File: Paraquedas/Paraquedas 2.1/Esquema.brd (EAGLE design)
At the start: 67.5 x 58.3 mm, 20 parts, among them Q1 IRF540, Q2 IRF540, Q3 IRF540

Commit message: Message
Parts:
- removed LED3: 5mm, led:LED5MM
- removed R8: 220, rcl:0207/10
- added LED2: 5mm, led:LED5MM
- added R7: 1k, rcl:0207/10
- R1, R5: value 220 -> 1k
- moved R4 97.4 mm to (-14.0, 11.4)
- moved R2 96.9 mm to (-14.0, 1.27), flipped to the bottom, turned to 180 degrees
- moved R3 96.7 mm to (-14.0, 6.35)
- moved LED1 47.7 mm to (13.5, 33.9), turned to 0 degrees
- moved R5 47.2 mm to (5.08, 40.6), turned to 270 degrees
- moved Q2 46.4 mm to (55.9, 25.4), flipped to the top
- moved SKIB2 46.4 mm to (55.9, 49.5), flipped to the top
- moved U$2 42.0 mm to (53.3, 6.35)
- moved R6 39.1 mm to (12.7, 26.0)
- moved R1 38.3 mm to (13.6, 50.3)
- moved OK2 36.8 mm to (15.2, 17.8)
- moved OK1 36.7 mm to (15.2, 43.2)
- moved U$1 25.0 mm to (44.5, 6.35)
- moved Q1 21.2 mm to (43.2, 25.4), flipped to the top
- moved SKIB1 21.2 mm to (43.2, 49.5), flipped to the top
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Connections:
- removed net N$3 (its old number): LED3.A, R8.2
- new net N$1: LED2.A, R7.2
- net GND: now also LED2.K; no longer LED3.K
- net SINAL_SKIB1: no longer R5.1
- net SINAL_SKIB2: no longer R8.1
- net SKIB1: now also U$2.1; no longer U$2.2
- net SKIB1_CONECTOR: now also R5.1
- net SKIB2: now also U$2.2; no longer U$2.1
- net SKIB2_CONECTOR: now also R7.1
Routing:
- net GND: track 0.00 -> 22.9 mm, vias 0 -> 4
- net SKIB1_CONECTOR: track 68.0 -> 89.4 mm
- net SKIB2_CONECTOR: track 77.3 -> 98.1 mm
- net 3.3V: track 68.2 -> 88.0 mm
- net SINAL_SKIB2: track 13.6 -> 0.00 mm
- net SINAL_SKIB1: track 13.2 -> 0.00 mm
- net N$1: track 0.00 -> 9.23 mm
- net N$3 (its old number): track 6.07 -> 0.00 mm
- net VCC: track 80.5 -> 86.2 mm
- net N$4: track 13.9 -> 11.1 mm
- net N$3: track 5.99 -> 7.80 mm
- net SKIB2: track 11.8 -> 13.2 mm
- net BUZZER: track 24.7 -> 23.5 mm
- net N$5: track 12.9 -> 11.8 mm
- net SKIB1: track 19.0 -> 19.7 mm
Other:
- board size 67.5 x 58.3 mm -> 66 x 57.2 mm

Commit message: Update paraquedas
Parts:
- removed LED1, LED2: 5mm, led:LED5MM
- removed OK1: PC817, optocoupler:DIL04
- added GND: PC817, optocoupler:DIL04
- added LSKIB1, LSKIB2: 5mm, led:LED5MM
- moved BATERIA 22.9 mm to (54.9, 7.37)
- moved R7 14.0 mm to (19.2, 18.2)
- moved R5 12.7 mm to (17.8, 40.6)
- moved U$1 8.98 mm to (35.6, 7.62), turned to 180 degrees
- moved U$2 8.98 mm to (44.5, 7.62)
- moved OK2 4.02 mm to (11.4, 19.1), turned to 270 degrees
- moved R1 3.41 mm to (10.5, 48.8), turned to 0 degrees
- moved R6 1.27 mm to (14.0, 26.0), turned to 0 degrees
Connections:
- net 3.3V: now also GND.4; no longer OK1.4
- net GND: now also GND.2, LSKIB1.K, LSKIB2.K; no longer LED1.K, LED2.K, OK1.2
- net N$1: now also LSKIB2.A; no longer LED2.A
- net N$3: now also LSKIB1.A; no longer LED1.A
- net N$4: now also GND.1; no longer OK1.1
- net SINAL_SKIB1: now also GND.3; no longer OK1.3
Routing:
- net 3.3V: track 88.0 -> 58.8 mm
- net GND: track 22.9 -> 0.00 mm, vias 4 -> 15
- net SKIB2_CONECTOR: track 98.1 -> 86.0 mm
- net SKIB1: track 19.7 -> 12.5 mm
- net N$5: track 11.8 -> 6.24 mm
- net N$4: track 11.1 -> 5.96 mm
- net BUZZER: track 23.5 -> 18.8 mm
- net N$1: track 9.23 -> 5.15 mm
- net VCC: track 86.2 -> 82.6 mm
- net SKIB1_CONECTOR: track 89.4 -> 92.4 mm
- net SKIB2: track 13.2 -> 14.6 mm
- net N$3: track 7.80 -> 6.74 mm
- net N$2: track 31.8 -> 32.8 mm
- added copper zone on layer 1, net GND

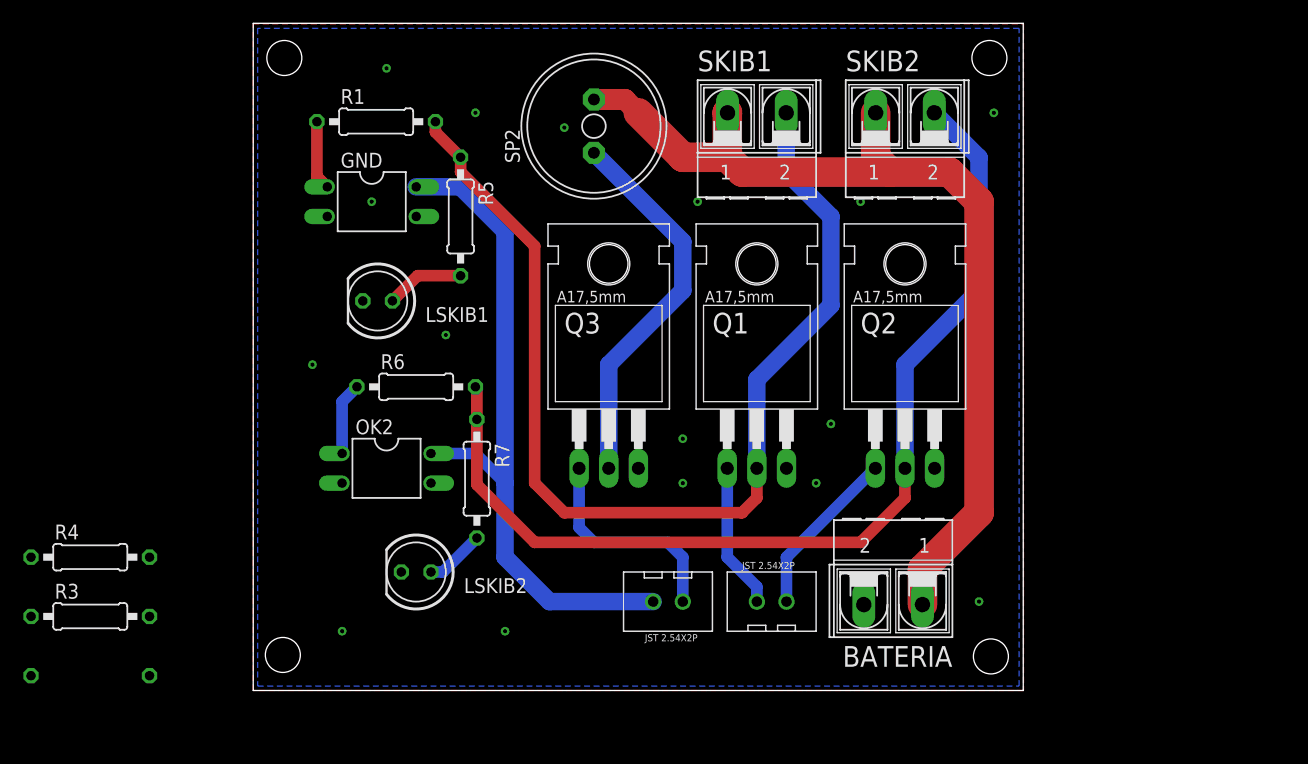
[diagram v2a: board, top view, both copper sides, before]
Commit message: correções avionica e paraquedas
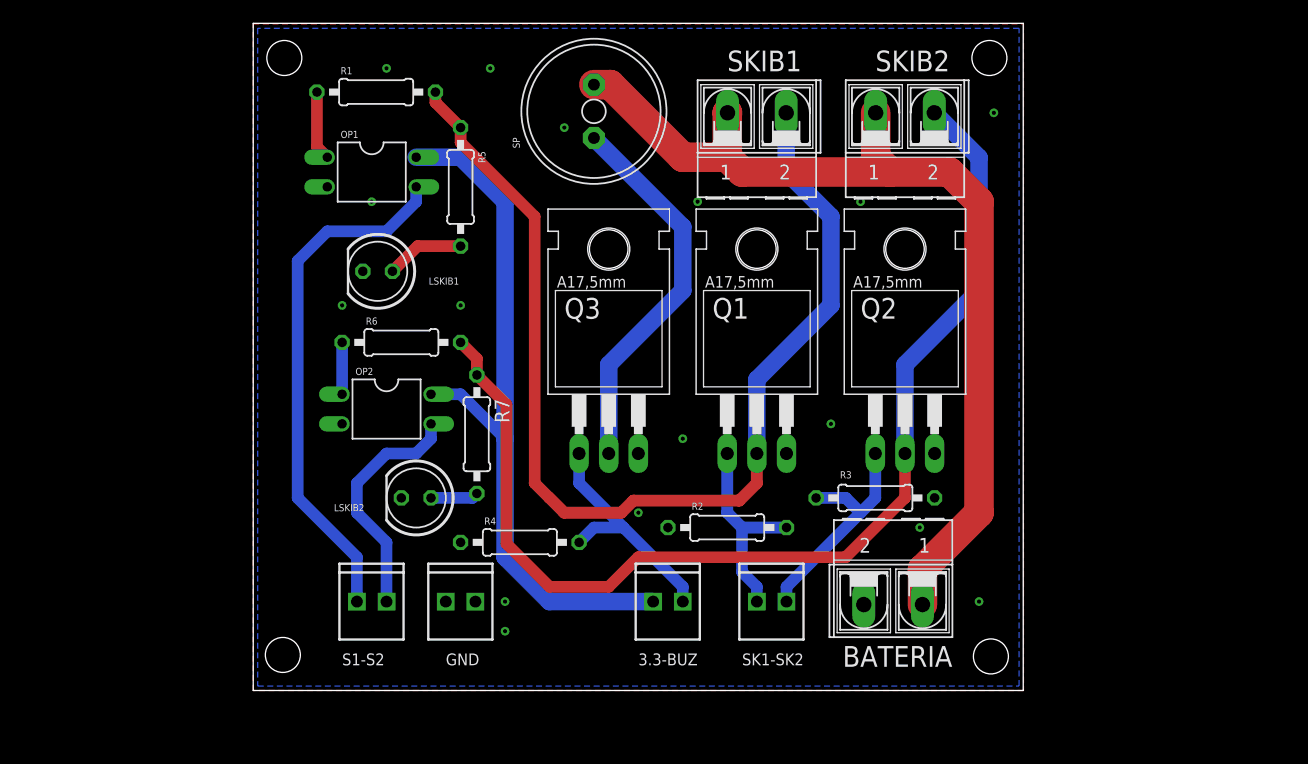
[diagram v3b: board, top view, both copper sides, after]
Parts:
- removed OK2: PC817, optocoupler:DIL04
- removed SP2: AL11P, buzzer:AL11P
- removed U$1, U$2: JST2.54X2P, CRD:JST2.54X2P_FOOTPRINT
- added 3.3-BUZ, S1-S2, SK1-SK2: (no value), SparkFun-Connectors:1X02_2.54_SCREWTERM
- added OP1, OP2: PC817, optocoupler:DIL04
- added SP: AL11P, buzzer:AL11P
- GND: value PC817 -> (none); device optocoupler:DIL04 -> SparkFun-Connectors:1X02_2.54_SCREWTERM
- moved R3 68.1 mm to (53.3, 16.5), turned to 180 degrees
- moved R2 56.1 mm to (40.6, 14.0), flipped to the top, turned to 0 degrees
- moved R4 36.9 mm to (22.9, 12.7)
- moved GND 34.9 mm to (16.5, 7.62), turned to 0 degrees
- moved LSKIB2 6.35 mm to (14.0, 16.5)
- moved R6 4.02 mm to (12.7, 29.8)
- moved R7 3.81 mm to (19.2, 22.0)
- moved LSKIB1 2.54 mm to (10.7, 35.9)
- moved R1 2.54 mm to (10.5, 51.3)
- moved R5 2.54 mm to (17.8, 43.2)
- moved Q1 1.27 mm to (43.2, 26.7)
- moved Q2 1.27 mm to (55.9, 26.7)
- moved Q3 1.27 mm to (30.5, 26.7)
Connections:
- net 3.3V: now also 3.3-BUZ.P2, OP1.4, OP2.4; no longer GND.4, OK2.4, U$1.2
- net BUZZER: now also 3.3-BUZ.P1, R4.2; no longer U$1.1
- net GND: now also GND.P1, GND.P2, OP1.2, OP2.2, R2.1, R3.1, R4.1; no longer GND.2, OK2.2
- net N$2: now also SP.-; no longer SP2.-
- net N$4: now also OP1.1; no longer GND.1
- net N$5: now also OP2.1; no longer OK2.1
- net SINAL_SKIB1: now also OP1.3, S1-S2.P2; no longer GND.3
- net SINAL_SKIB2: now also OP2.3, S1-S2.P1; no longer OK2.3
- net SKIB1: now also R2.2, SK1-SK2.P2; no longer U$2.1
- net SKIB2: now also R3.2, SK1-SK2.P1; no longer U$2.2
- net VCC: now also SP.+; no longer SP2.+
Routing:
- net SINAL_SKIB1: track 0.00 -> 44.8 mm
- net SINAL_SKIB2: track 0.00 -> 20.4 mm
- net SKIB2_CONECTOR: track 86.0 -> 95.0 mm
- net SKIB2: track 14.6 -> 20.2 mm
- net SKIB1: track 12.5 -> 17.6 mm
- net 3.3V: track 58.8 -> 61.9 mm
- net BUZZER: track 18.8 -> 20.7 mm
- net SKIB1_CONECTOR: track 92.4 -> 94.2 mm
- net N$5: track 6.24 -> 4.45 mm
- net N$1: track 5.15 -> 4.09 mm
- net VCC: track 82.6 -> 83.2 mm
